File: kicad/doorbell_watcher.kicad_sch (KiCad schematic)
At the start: 25 parts, among them J1 Screw Terminal, J2 TinyPICO ESP32 header, J3 Conn_01x10, U1 LM2596S-5, U2 PC817

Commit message: Added button signal simulation. Schematic is complete.
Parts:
- removed D3: MBR0520, Diode_SMD:D_SOD-123, symbol Diode:MBR0520
- added C4: 100n, symbol Device:C
- added D2: DF01S1, Diode_SMD:Diode_Bridge_OnSemi_SDIP-4L, symbol Diode_Bridge:DF01S1
- added R4: 50K, symbol Device:R
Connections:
- net C1: now also D2.4; no longer R1.1
- net GND: now also C4.2
- net Vin1: now also D2.3; no longer U2.2
- net at R2.1, TP10.1, U2.4: now also C4.1, R4.1
- net +3V3: now reaches J2.17 (Pin_17)
- net +3V3: now also R4.2
- new net: D2.2 (-), U2.2
- new net: D2.1 (+), R1.1
- no-connect marks 3 -> 2
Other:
- moved on the sheet: TP10, TP9, U2

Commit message: Placement done
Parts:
- removed C3: 680u, symbol Device:C_Polarized
- removed D2: DF01S1, Diode_SMD:Diode_Bridge_OnSemi_SDIP-4L, symbol Diode_Bridge:DF01S1
- removed J2: TinyPICO ESP32 header, symbol Connector_Generic:Conn_02x10_Counter_Clockwise
- removed TP6: ~, symbol Connector:TestPoint
- removed U2: PC817, Package_DIP:DIP-4_W7.62mm, symbol Isolator:PC817
- added J2, J4: Conn_01x10, parts_lib:10-pin header, symbol Connector_Generic:Conn_01x10
- added TP4: ~, TestPoint:TestPoint_Pad_D2.0mm, symbol Connector:TestPoint
- added U1: ACPL-214-500E, Package_SO:SOP-4_4.4x2.6mm_P1.27mm, symbol Isolator:ACPL-214-500E
- C2: renamed from C1; footprint (none) -> parts_lib:CAP_EEFK_J16_PAN-M
- C3: renamed from C4; footprint (none) -> Capacitor_SMD:C_0805_2012Metric_Pad1.18x1.45mm_HandSolder
- C4: renamed from C2; footprint (none) -> parts_lib:CAP_EEFK_F_PAN-M
- D2: renamed from D1; footprint Diode_SMD:D_SMA -> parts_lib:ss24_do214AC
- J1: footprint (none) -> parts_lib:screw_connector_1x3
- J3: footprint (none) -> parts_lib:10-pin header; now left out of the parts list
- L1: footprint (none) -> parts_lib:IND_829SNLT_PUL
- R1: footprint (none) -> Resistor_SMD:R_0805_2012Metric_Pad1.20x1.40mm_HandSolder
- R2: renamed from R4; footprint (none) -> Resistor_SMD:R_0805_2012Metric_Pad1.20x1.40mm_HandSolder
- R3: renamed from R2; footprint (none) -> Resistor_SMD:R_0805_2012Metric_Pad1.20x1.40mm_HandSolder
- R4: renamed from R3; footprint (none) -> Resistor_SMD:R_0805_2012Metric_Pad1.20x1.40mm_HandSolder
- TP1: renamed from TP9; footprint (none) -> TestPoint:TestPoint_Pad_D2.0mm; now left out of the parts list
- TP10: renamed from TP2; footprint (none) -> TestPoint:TestPoint_Pad_D2.0mm; now left out of the parts list
- TP11: renamed from TP3; footprint (none) -> TestPoint:TestPoint_Pad_D2.0mm; now left out of the parts list
- TP3: renamed from TP10; footprint (none) -> TestPoint:TestPoint_Pad_D2.0mm; now left out of the parts list
- TP5: renamed from TP8; footprint (none) -> TestPoint:TestPoint_Pad_D2.0mm; now left out of the parts list
- TP6: renamed from TP7; footprint (none) -> TestPoint:TestPoint_Pad_D2.0mm; now left out of the parts list
- TP7: renamed from TP4; footprint (none) -> TestPoint:TestPoint_Pad_D2.0mm; now left out of the parts list
- TP8: renamed from TP5; footprint (none) -> TestPoint:TestPoint_Pad_D2.0mm; now left out of the parts list
- TP9: renamed from TP1; footprint (none) -> TestPoint:TestPoint_Pad_D2.0mm; now left out of the parts list
- renumbered D7 to D1, U1 to U2
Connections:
- net +3V3: now also J4.4 (Pin_4)
- net +5V: now also J4.3 (Pin_3)
- net C1: now also R1.1
- net GND: now also J2.10 (Pin_10), J4.2 (Pin_2), U1.3
- net IO14: now also J4.6 (Pin_6)
- net IO15: now also J4.7 (Pin_7)
- net IO18: now also J2.3 (Pin_3)
- net IO19: now also J2.2 (Pin_2)
- net IO21: now also J2.6 (Pin_6)
- net IO22: now also J2.5 (Pin_5)
- net IO23: now also J2.1 (Pin_1)
- net IO25: now also J4.10 (Pin_10)
- net IO26: now also J4.9 (Pin_9)
- net IO27: now also J4.8 (Pin_8)
- net IO32: now also J2.7 (Pin_7)
- net IO33: now also J2.8 (Pin_8)
- net IO4: now also J4.5 (Pin_5)
- net IO5: now also J2.4 (Pin_4)
- net Vin1: now also U1.2
- net at C3.1, R2.1, R3.1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: now also TP4.1, U1.4
- net at R1.2, TP1.1: now also U1.1
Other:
- moved on the sheet: C2, C3, C4, D1, D2, L1, R1, R2, R3, TP1, TP3, TP5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

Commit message: Routing complete, changed LM2596 to LM2594
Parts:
- removed C2: 680u, parts_lib:CAP_EEFK_J16_PAN-M, symbol Device:C_Polarized
- removed J3: Conn_01x10, parts_lib:10-pin header, symbol Connector_Generic:Conn_01x10
- removed TP1, TP10, TP11, TP3, TP4, TP5, TP6, TP7, TP8, TP9: ~, TestPoint:TestPoint_Pad_D2.0mm, symbol Connector:TestPoint
- removed U2: LM2596S-5, Package_TO_SOT_SMD:TO-263-5_TabPin3, symbol Regulator_Switching:LM2596S-5
- added C1: 220u, parts_lib:CAP_EEFK_F_PAN-M, symbol Device:C_Polarized
- added U2: LM2594M-5.0, Package_SO:SOIC-8_3.9x4.9mm_P1.27mm, symbol Regulator_Switching:LM2594M-5.0
- renumbered C3 to C2, C4 to C3, J4 to J3
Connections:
- net +5V: now also U2.4 (FB)
- net GND: now also C1.2, U2.5 (~{ON}/OFF), U2.6 (GND)
- net at D2.1 (K), L1.1: now also U2.8 (OUT)
- net at D1.1 (+): now also C1.1, U2.7 (VIN)
- net IO15: no longer names the net of J3.7 (Pin_7)
- net IO25: no longer names the net of J3.10 (Pin_10)
- net IO26: no longer names the net of J3.9 (Pin_9)
- net IO27: no longer names the net of J3.8 (Pin_8)
- no-connect marks 2 -> 9
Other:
- moved on the sheet: J2, J3, R4

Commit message: Added fabrication files
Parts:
- D1: value DF01S1 -> MDB10S
- J1: value Screw Terminal -> Screw Terminal 01x03
- U2: value LM2594M-5.0 -> LM2594MX-5.0
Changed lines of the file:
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@@
 			)
 		)
-		(property "Value" "Screw Terminal"
+		(property "Value" "Screw Terminal 01x03"
 			(at 100.33 45.72 0)
 			(effects
@@
 			)
 		)
-		(property "Value" "LM2594M-5.0"
+		(property "Value" "LM2594MX-5.0"
 			(at 86.36 96.52 0)
 			(effects
@@
 			)
 		)
-		(property "Value" "DF01S1"
+		(property "Value" "MDB10S"
 			(at 52.07 97.7198 0)
 			(effects

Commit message: First fabrication release done
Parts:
- C1, C3: footprint parts_lib:CAP_EEFK_F_PAN-M -> parts_lib:CAP_FT_F_PAN-M; LCSC (none) -> C178594
- C2: LCSC (none) -> C49678
- D1: LCSC (none) -> C258169
- D2: LCSC (none) -> C211773
- J1: LCSC (none) -> C589616
- J2, J3: LCSC (none) -> C225507
- L1: LCSC (none) -> C2453068
- R1, R3: LCSC (none) -> C17630
- R2: LCSC (none) -> C2828840
- R4: LCSC (none) -> C17477
- U1: LCSC (none) -> C5361360
- U2: LCSC (none) -> C35323
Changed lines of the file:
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@@
+			)
+		)
+		(property "LCSC" "C17477"
+			(at 207.01 124.46 90)
+			(effects
+				(font
+					(size 1.27 1.27)
+				)
+				(hide yes)
 			)
 		)
@@
 			)
 		)
+		(property "LCSC" "C211773"
+			(at 111.76 113.03 90)
+			(effects
+				(font
+					(size 1.27 1.27)
+				)
+				(hide yes)
+			)
+		)
 		(pin "2"
 		)
@@
 			)
 		)
+		(property "LCSC" "C2828840"
+			(at 95.25 153.67 0)
+			(effects
+				(font
+					(size 1.27 1.27)
+				)
+				(hide yes)
+			)
+		)
 		(pin "2"
 		)
@@
 			)
 		)
+		(property "LCSC" "C5361360"
+			(at 72.39 161.29 0)
+			(effects
+				(font
+					(size 1.27 1.27)
+				)
+				(hide yes)
+			)
+		)
 		(pin "1"
 		)
@@
 		(property "Sim.Pins" ""
 			(at 118.11 106.68 0)
+			(effects
+				(font
+					(size 1.27 1.27)
+				)
+				(hide yes)
+			)
+		)
+		(property "LCSC" "C2453068"
+			(at 118.11 106.68 90)
 			(effects
 				(font
@@
 			)
 		)
+		(property "LCSC" "C589616"
+			(at 100.33 52.07 0)
+			(effects
+				(font
+					(size 1.27 1.27)
+				)
+				(hide yes)
+			)
+		)
 		(pin "2"
 		)
@@
 			)
 		)
+		(property "LCSC" "C35323"
+			(at 86.36 104.14 0)
+			(effects
+				(font
+					(size 1.27 1.27)
+				)
+				(hide yes)
+			)
+		)
 		(pin "6"
 		)
@@
 			)
 		)
+		(property "LCSC" "C225507"
+			(at 210.82 74.93 0)
+			(effects
+				(font
+					(size 1.27 1.27)
+				)
+				(hide yes)
+			)
+		)
 		(pin "9"
 		)
@@
 			)
 		)
+		(property "LCSC" "C17630"
+			(at 107.95 158.75 90)
+			(effects
+				(font
+					(size 1.27 1.27)
+				)
+				(hide yes)
+			)
+		)
 		(pin "2"
 		)
@@
 			)
 		)
+		(property "LCSC" "C49678"
+			(at 90.17 163.83 0)
+			(effects
+				(font
+					(size 1.27 1.27)
+				)
+				(hide yes)
+			)
+		)
 		(pin "2"
 		)
@@
 			)
 		)
+		(property "LCSC" "C225507"
+			(at 199.39 74.93 0)
+			(effects
+				(font
+					(size 1.27 1.27)
+				)
+				(hide yes)
+			)
+		)
 		(pin "9"
 		)
@@
 			)
 		)
-		(property "Footprint" "parts_lib:CAP_EEFK_F_PAN-M"
+		(property "Footprint" "parts_lib:CAP_FT_F_PAN-M"
 			(at 127.9652 116.84 0)
 			(effects
@@
 		)
 		(property "Sim.Pins" ""
+			(at 127 113.03 0)
+			(effects
+				(font
+					(size 1.27 1.27)
+				)
+				(hide yes)
+			)
+		)
+		(property "LCSC" "C178594"
 			(at 127 113.03 0)
 			(effects
@@
 			)
 		)
-		(property "Footprint" "parts_lib:CAP_EEFK_F_PAN-M"
+		(property "Footprint" "parts_lib:CAP_FT_F_PAN-M"
 			(at 62.5348 113.03 0)
 			(effects
@@
 		)
 		(property "Sim.Pins" ""
+			(at 63.5 109.22 0)
+			(effects
+				(font
+					(size 1.27 1.27)
+				)
+				(hide yes)
+			)
+		)
+		(property "LCSC" "C178594"
 			(at 63.5 109.22 0)
 			(effects
@@
 			)
 		)
+		(property "LCSC" "C258169"
+			(at 41.91 101.6 0)
+			(effects
+				(font
+					(size 1.27 1.27)
+				)
+				(hide yes)
+			)
+		)
 		(pin "4"
 		)
@@
 			(effects
 				(font
+					(size 1.27 1.27)
+				)
+				(hide yes)
+			)
+		)
+		(property "LCSC" "C17630"
+			(at 49.53 158.75 90)
+			(effects
+				(font

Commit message: Fix MDB9S footprint
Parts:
- D1: footprint Diode_SMD:Diode_Bridge_OnSemi_SDIP-4L -> parts_lib:TSSOP4-MICRO-DIP_948BS_ONS-M
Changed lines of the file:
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@@
 			)
 		)
-		(property "Footprint" "Diode_SMD:Diode_Bridge_OnSemi_SDIP-4L"
+		(property "Footprint" "parts_lib:TSSOP4-MICRO-DIP_948BS_ONS-M"
 			(at 45.72 98.425 0)
 			(effects

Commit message: Fix unconnected 5V pin in ESP32 header
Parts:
- D2: footprint parts_lib:ss24_do214AC -> parts_lib:DO-214AC(SMA)
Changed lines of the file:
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@@
 			)
 		)
-		(property "Footprint" "parts_lib:ss24_do214AC"
+		(property "Footprint" "parts_lib:DO-214AC(SMA)"
 			(at 116.205 113.03 0)
 			(effects

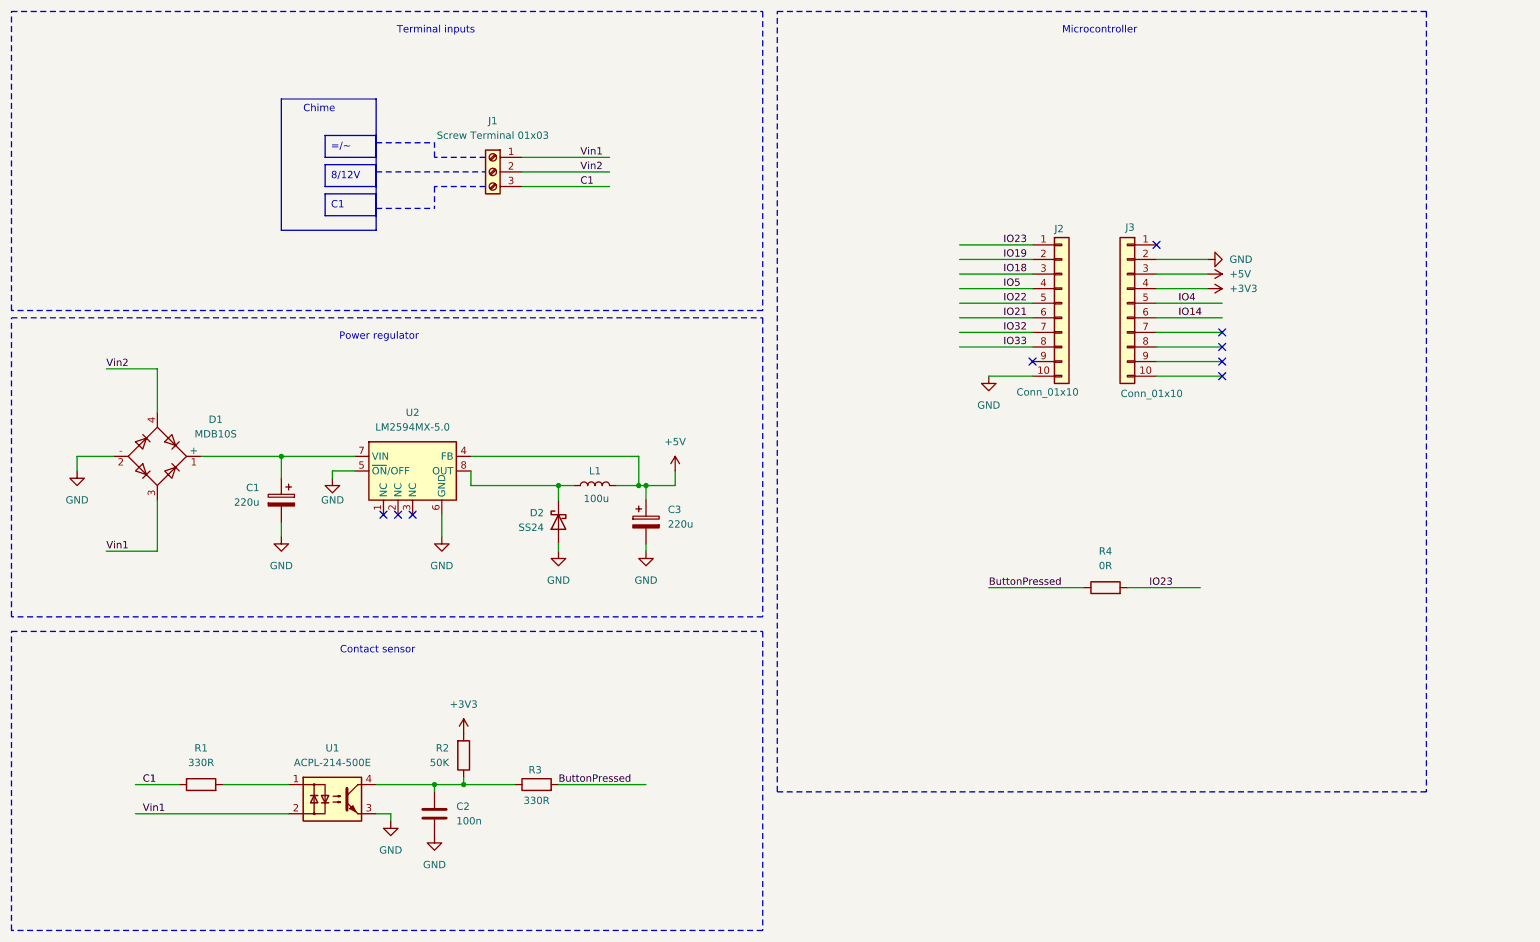
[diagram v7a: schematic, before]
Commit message: Add relay
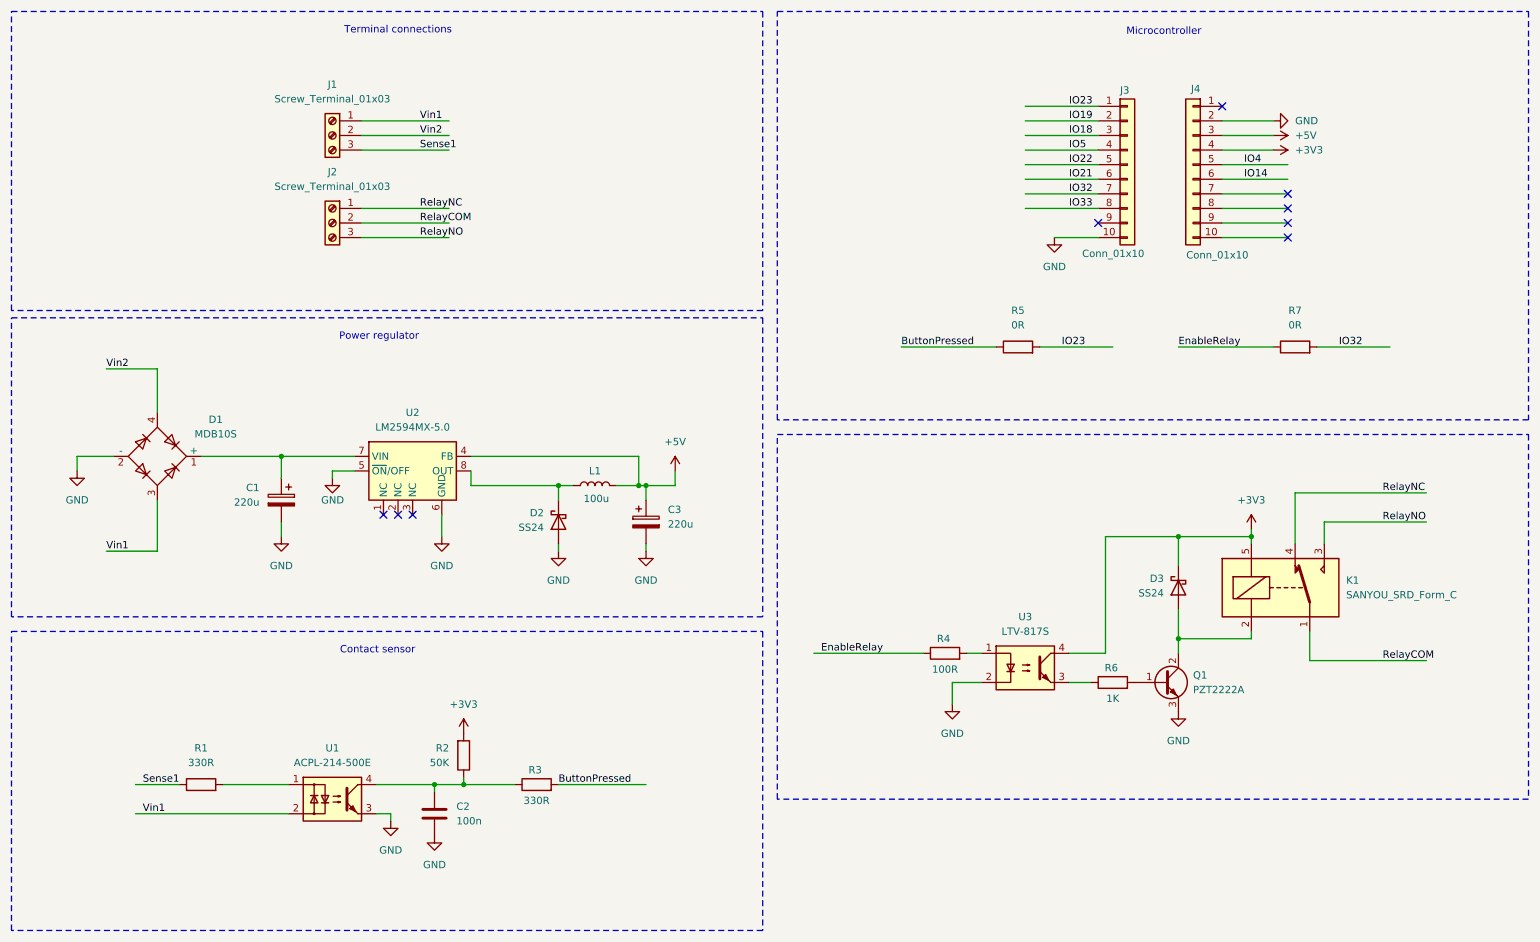
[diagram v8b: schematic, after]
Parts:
- added D3: SS24, parts_lib:DO-214AC(SMA), symbol Diode:SS24
- added J2: Screw_Terminal_01x03, parts_lib:screw_connector_1x3, symbol Connector:Screw_Terminal_01x03
- added K1: SANYOU_SRD_Form_C, Relay_THT:Relay_SPDT_SANYOU_SRD_Series_Form_C, symbol Relay:SANYOU_SRD_Form_C
- added Q1: PZT2222A, Package_TO_SOT_SMD:SOT-223-3_TabPin2, symbol Transistor_BJT:PZT2222A
- added R4: 100R, Resistor_SMD:R_0805_2012Metric_Pad1.20x1.40mm_HandSolder, symbol Device:R
- added R6: 1K, Resistor_SMD:R_0805_2012Metric_Pad1.20x1.40mm_HandSolder, symbol Device:R
- added R7: 0R, Resistor_SMD:R_0805_2012Metric_Pad1.20x1.40mm_HandSolder, symbol Device:R
- added U3: LTV-817S, Package_DIP:SMDIP-4_W9.53mm, symbol Isolator:LTV-817S
- J1: value Screw Terminal 01x03 -> Screw_Terminal_01x03
- renumbered J2 to J3, J3 to J4, R4 to R5
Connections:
- net +3V3: now also D3.1 (K), K1.5, U3.4
- net GND: now also Q1.3 (E), U3.2
- net IO32: now also R7.2
- net C1 renamed Sense1
- new net: R6.1, U3.3
- new net: Q1.1 (B), R6.2
- new net: D3.2 (A), K1.2, Q1.2 (C)
- new net: R4.2, U3.1
- new net EnableRelay: R4.1, R7.1
- new net RelayCOM: J2.2 (Pin_2), K1.1
- new net RelayNC: J2.1 (Pin_1), K1.4
- new net RelayNO: J2.3 (Pin_3), K1.3
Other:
- note added: "Terminal connections"
- note removed: "Chime"
- note removed: "Terminal inputs"
- moved on the sheet: J3, J4, R5
